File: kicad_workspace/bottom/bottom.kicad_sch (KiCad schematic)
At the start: 27 parts, among them J1 Battery connector, M1 N20_MOTOR_EXTENDED_SHAFT, M2 N20_MOTOR_EXTENDED_SHAFT, U1 DRV8833PWP, U2 ULTRASOUND_T_R, U3 ATmega4809-A, U4 BNO055, Y1 32.768kHz

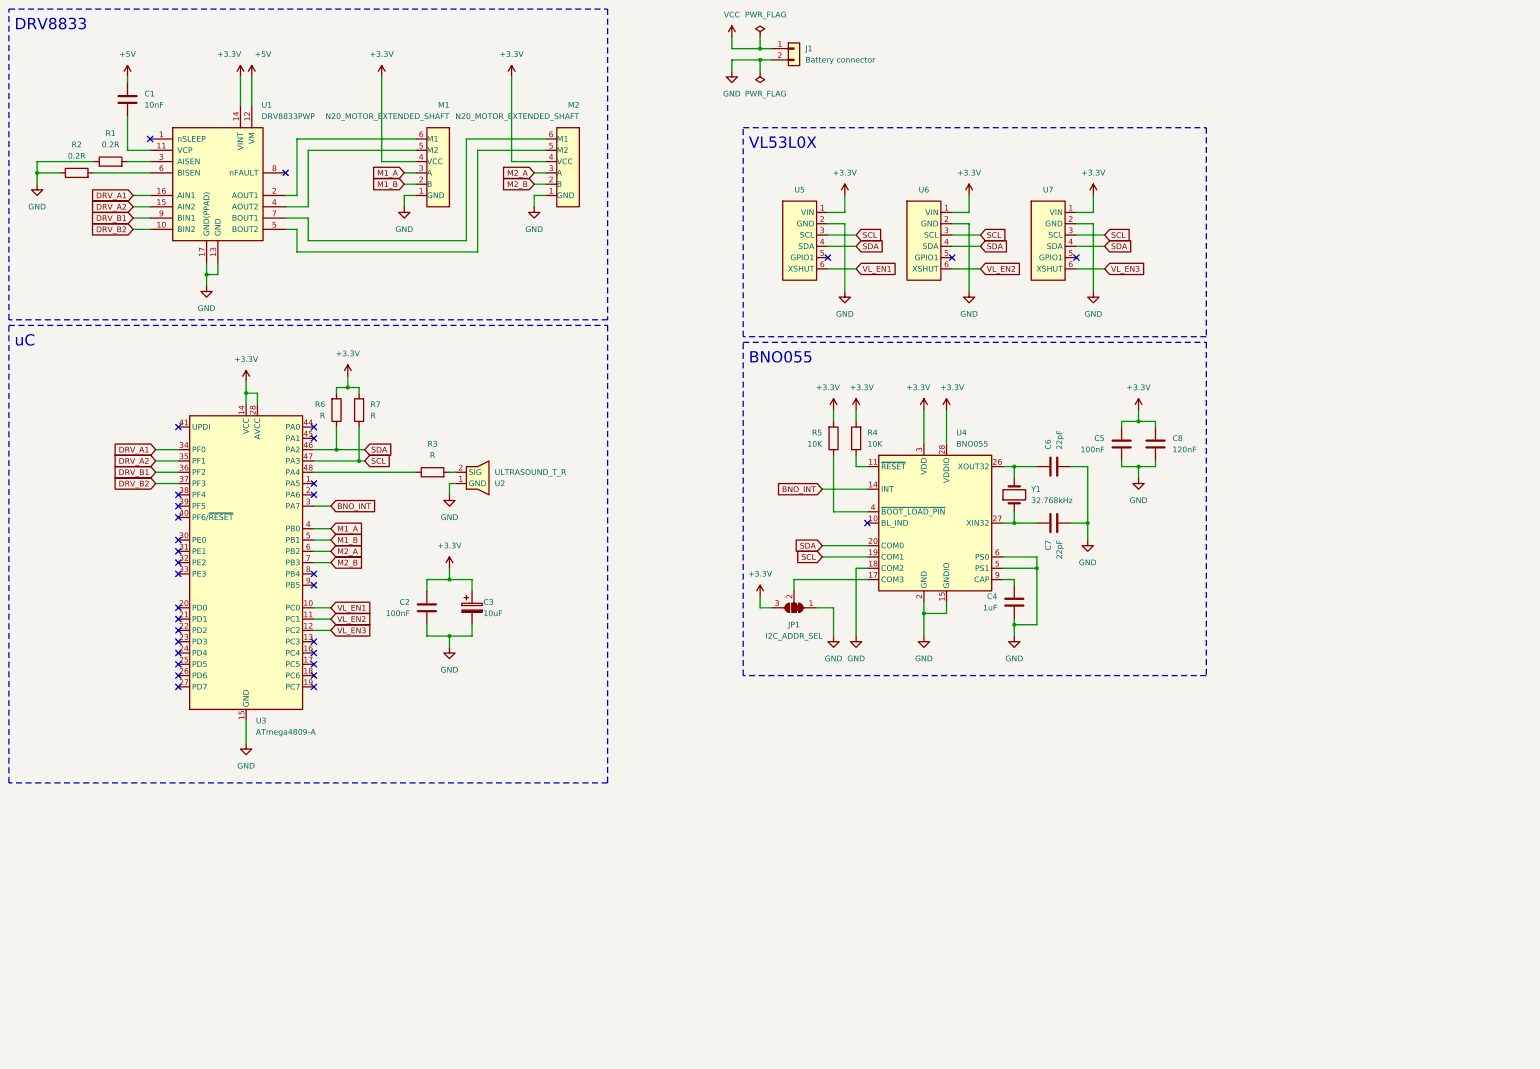
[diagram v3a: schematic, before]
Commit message: add dw01 and its mosfets to schematic and pcb
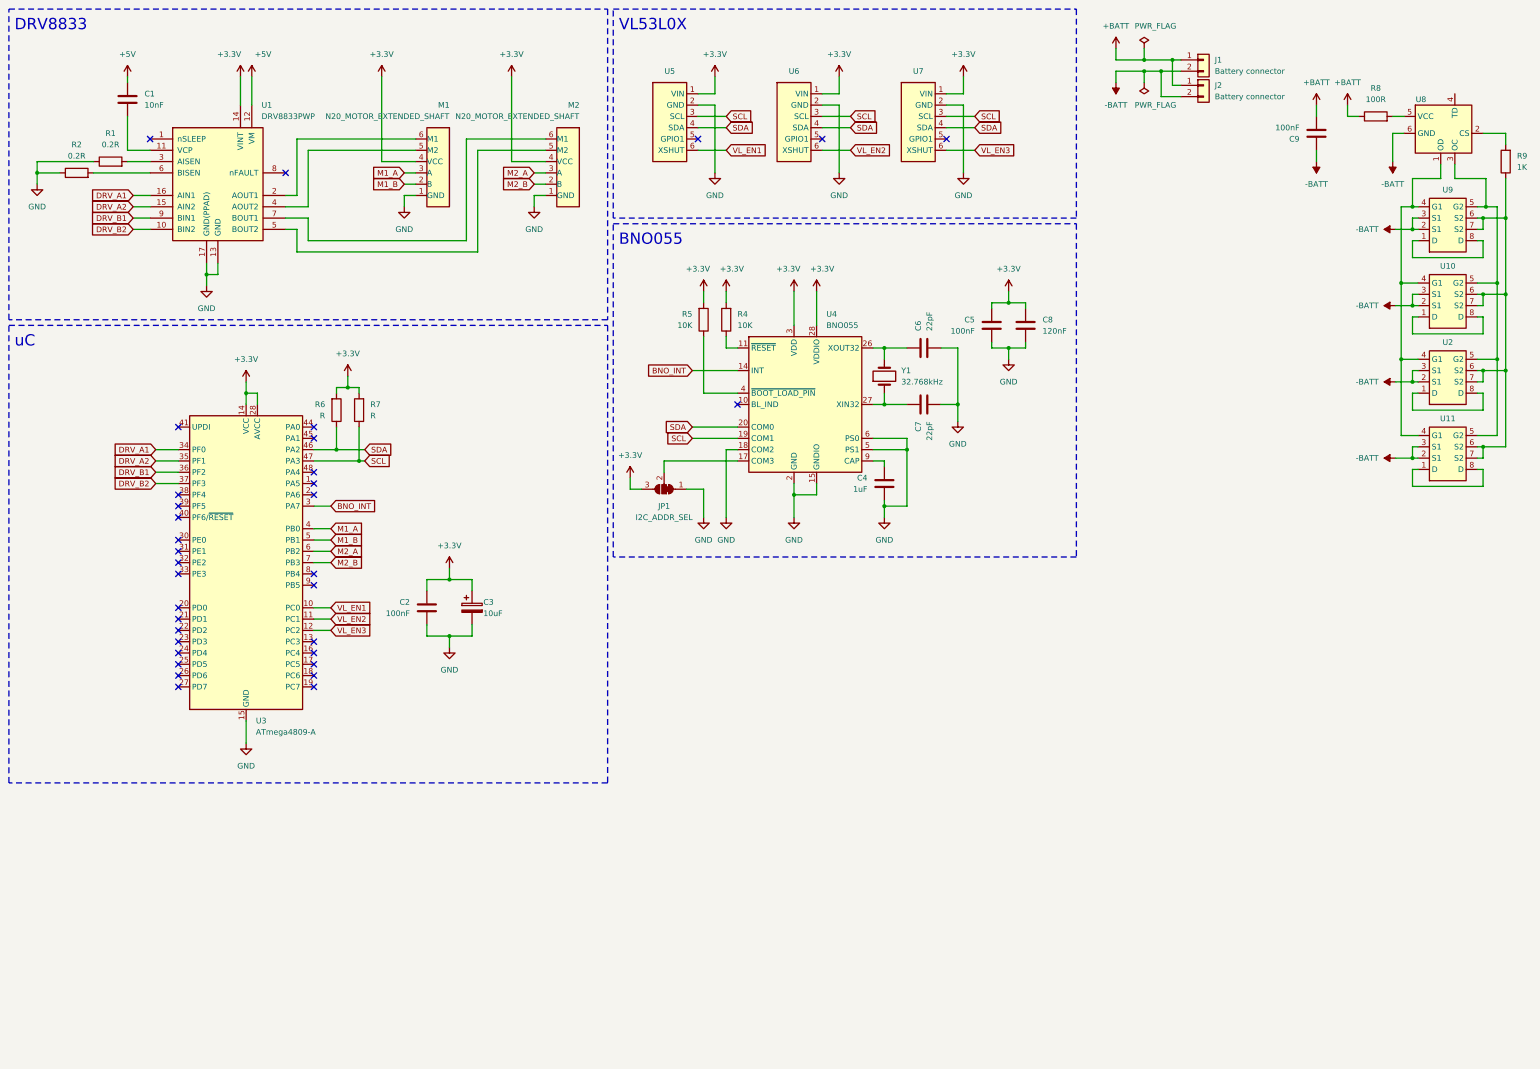
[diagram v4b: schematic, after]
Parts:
- removed R3: R, Resistor_SMD:R_0805_2012Metric, symbol Device:R
- removed U2: ULTRASOUND_T_R, pololu:ULTRASOUND_T_R, symbol pololu:ULTRASOUND_T_R
- added C9: 100nF, Capacitor_SMD:C_0805_2012Metric, symbol Device:C
- added J2: Battery connector, Connector_JST:JST_XH_B2B-XH-AM_1x02_P2.50mm_Vertical, symbol Connector_Generic:Conn_01x02
- added R8: 100R, Resistor_SMD:R_0805_2012Metric, symbol Device:R
- added R9: 1K, Resistor_SMD:R_0805_2012Metric, symbol Device:R
- added U10, U11, U2, U9: ~, Package_SO:TSSOP-8_4.4x3mm_P0.65mm, symbol pololu:8205A
- added U8: ~, Package_TO_SOT_SMD:SOT-23-6, symbol pololu:DW01
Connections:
- net GND: no longer J1.2 (Pin_2)
- net VCC renamed +BATT
- net +BATT: now also C9.2, J2.1 (Pin_1), R8.1
- new net: U2.1 (D), U2.8 (D)
- new net: U10.4 (G1), U11.4 (G1), U2.4 (G1), U8.1 (OD), U9.4 (G1)
- new net: U10.5 (G2), U11.5 (G2), U2.5 (G2), U8.3 (OC), U9.5 (G2)
- new net: R9.1, U10.6 (S2), U10.7 (S2), U11.6 (S2), U11.7 (S2), U2.6 (S2), U2.7 (S2), U9.6 (S2), U9.7 (S2)
- new net: U9.1 (D), U9.8 (D)
- new net: R8.2, U8.5 (VCC)
- new net: U10.1 (D), U10.8 (D)
- new net: U11.1 (D), U11.8 (D)
- new net: R9.2, U8.2 (CS)
- new net -BATT: C9.1, J1.2 (Pin_2), J2.2 (Pin_2), U10.2 (S1), U10.3 (S1), U11.2 (S1), U11.3 (S1), U2.2 (S1), U2.3 (S1), U8.6 (GND), U9.2 (S1), U9.3 (S1)
- no-connect marks 33 -> 34
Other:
- moved on the sheet: C4, C5, C6, C7, C8, J1, JP1, R4, R5, U4, U5, U6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

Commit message: wired dw01 and 4x 8205a mosfets
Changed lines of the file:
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@@
+    (stroke (width 0) (type default))
+  )
+  (wire (pts (xy 350.52 52.07) (xy 350.52 60.96))
     (stroke (width 0) (type default))
   )
@@
     (stroke (width 0) (type default))
   )
-  (wire (pts (xy 350.52 60.96) (xy 350.52 52.07))
-    (stroke (width 0) (type default))
-  )

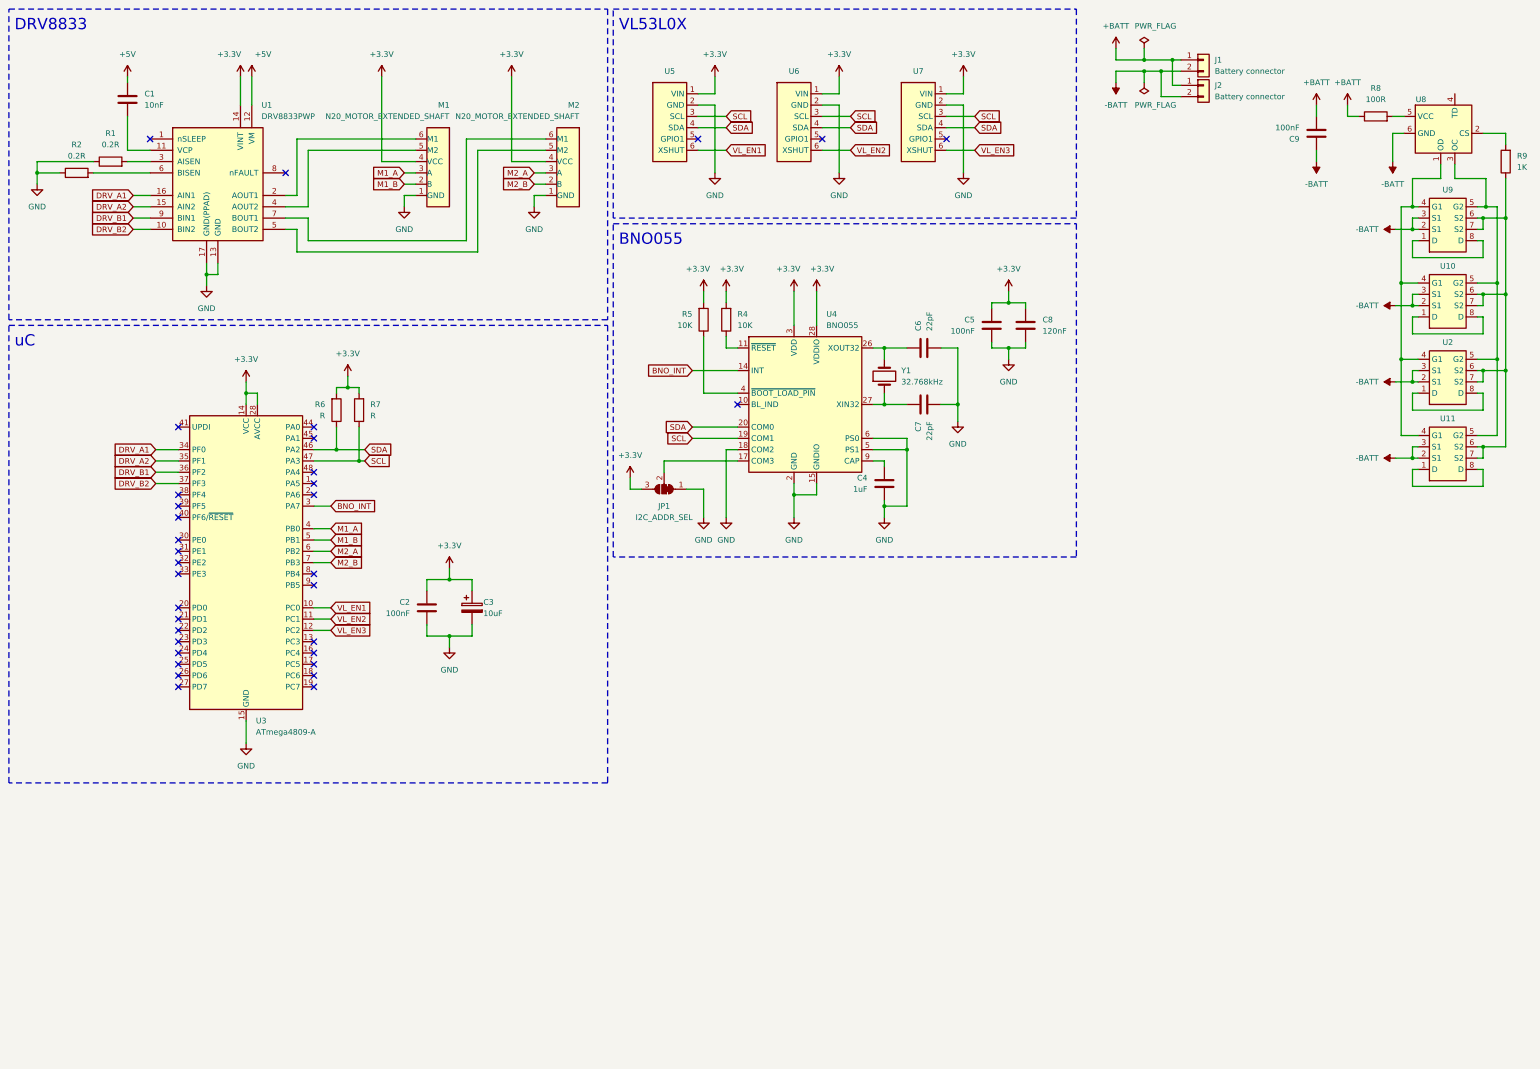
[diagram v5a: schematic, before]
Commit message: switch to stm32f303re uC
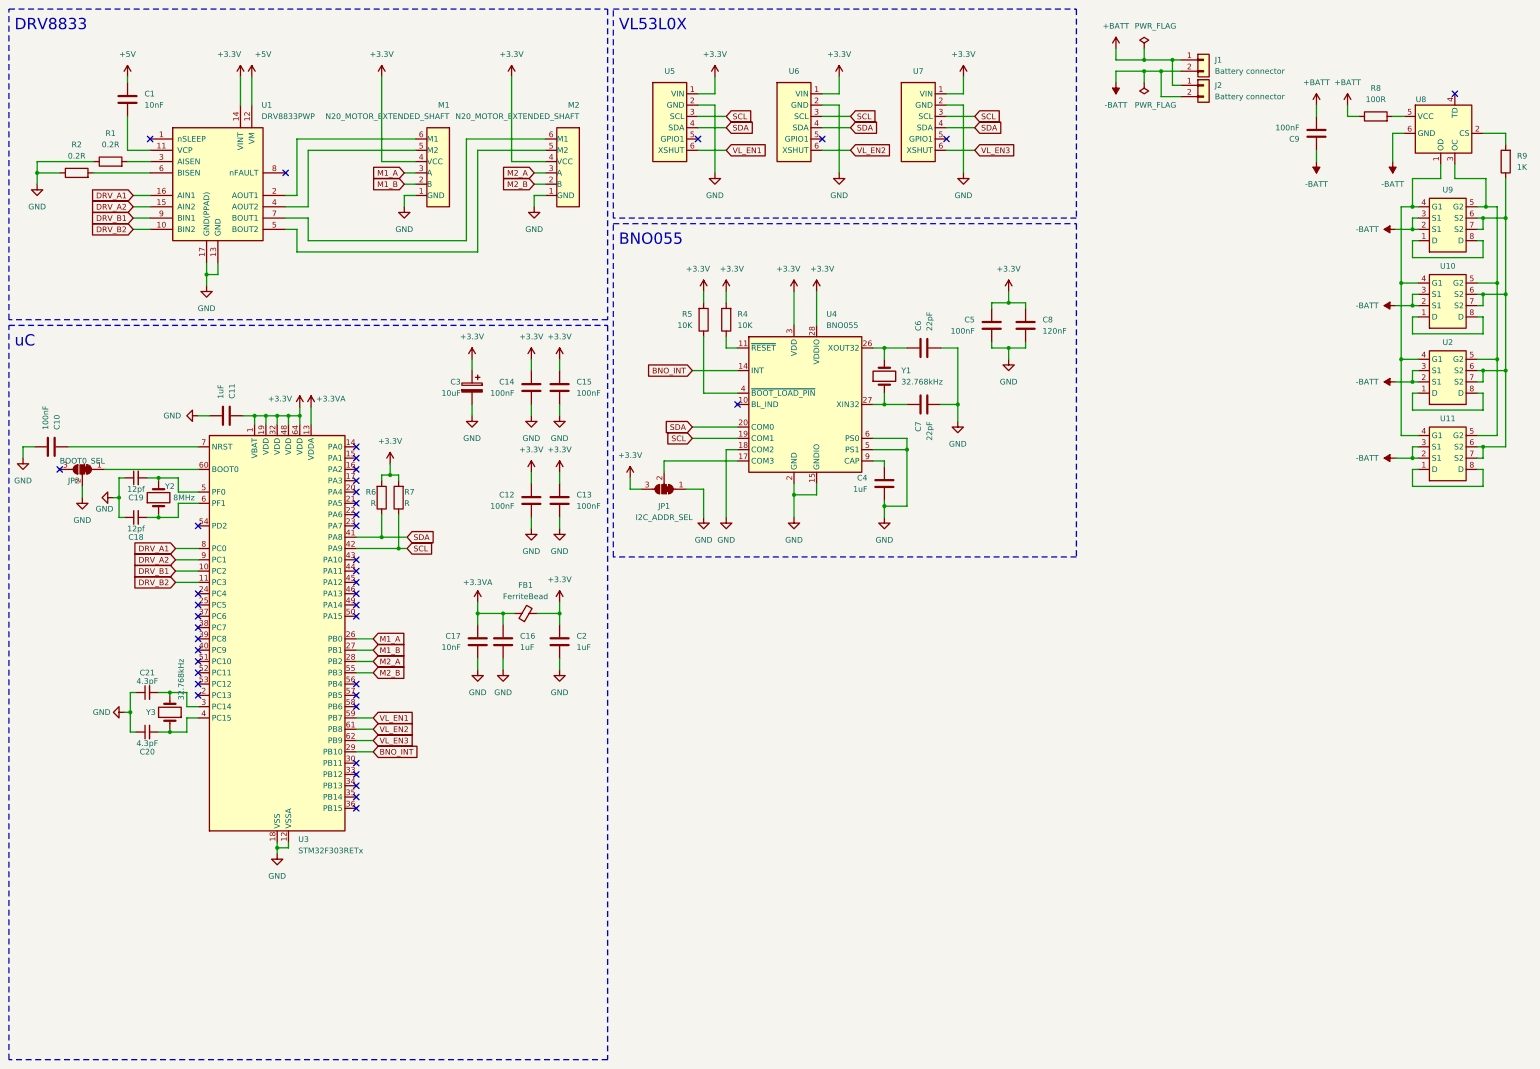
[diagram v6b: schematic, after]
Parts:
- removed U3: ATmega4809-A, Package_QFP:TQFP-48_7x7mm_P0.5mm, symbol MCU_Microchip_ATmega:ATmega4809-A
- added C10, C12, C13, C14, C15: 100nF, Capacitor_SMD:C_0805_2012Metric, symbol Device:C
- added C11, C16: 1uF, Capacitor_SMD:C_0805_2012Metric, symbol Device:C
- added C17: 10nF, Capacitor_SMD:C_0805_2012Metric, symbol Device:C
- added C18, C19: 12pf, Capacitor_SMD:C_0805_2012Metric, symbol Device:C_Small
- added C20, C21: 4.3pF, Capacitor_SMD:C_0805_2012Metric, symbol Device:C_Small
- added FB1: FerriteBead, Inductor_SMD:L_0805_2012Metric, symbol Device:FerriteBead_Small
- added JP2: BOOT0_SEL, Jumper:SolderJumper-3_P1.3mm_Bridged12_Pad1.0x1.5mm_NumberLabels, symbol Jumper:SolderJumper_3_Bridged12
- added U3: STM32F303RETx, Package_QFP:LQFP-64_10x10mm_P0.5mm, symbol MCU_ST_STM32F3:STM32F303RETx
- added Y2: 8MHz, Crystal:Crystal_SMD_MicroCrystal_CM9V-T1A-2Pin_1.6x1.0mm, symbol Device:Crystal
- added Y3: 32.768kHz, Crystal:Crystal_SMD_MicroCrystal_CM9V-T1A-2Pin_1.6x1.0mm, symbol Device:Crystal
- C2: value 100nF -> 1uF
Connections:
- net +3.3V: now also C11.1, C12.1, C13.1, C14.1, C15.1, FB1.2, U3.1 (VBAT), U3.19 (VDD), U3.32 (VDD), U3.48 (VDD), U3.64 (VDD)
- net BNO_INT: now also U3.29 (PB10)
- net DRV_A1: now also U3.8 (PC0)
- net DRV_A2: now also U3.9 (PC1)
- net DRV_B1: now also U3.10 (PC2)
- net DRV_B2: now also U3.11 (PC3)
- net GND: now also C10.2, C11.2, C12.2, C13.2, C14.2, C15.2, C16.2, C17.2, C18.1, C19.1, C20.1, C21.1, JP2.2 (C), U3.12 (VSSA), U3.18 (VSS), U3.31 (VSS), U3.47 (VSS), U3.63 (VSS)
- net M1_A: now also U3.26 (PB0)
- net M1_B: now also U3.27 (PB1)
- net M2_A: now also U3.28 (PB2)
- net M2_B: now also U3.55 (PB3)
- net SCL: now also U3.42 (PA9)
- net SDA: now also U3.41 (PA8)
- net VL_EN1: now also U3.59 (PB7)
- net VL_EN2: now also U3.61 (PB8)
- net VL_EN3: now also U3.62 (PB9)
- new net: C10.1, U3.7 (NRST)
- new net: JP2.1 (A), U3.60 (BOOT0)
- new net: C21.2, U3.3 (PC14), Y3.2
- new net: C18.2, U3.6 (PF1), Y2.1
- new net: C20.2, U3.4 (PC15), Y3.1
- new net: C19.2, U3.5 (PF0), Y2.2
- new net +3.3VA: C16.1, C17.1, FB1.1, U3.13 (VDDA)
- no-connect marks 34 -> 41
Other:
- moved on the sheet: C3, R6, R7
